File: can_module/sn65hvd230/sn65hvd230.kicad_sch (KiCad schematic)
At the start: 5 parts, among them J1 Conn_01x04, J2 Conn_01x02, U1 SN65HVD230

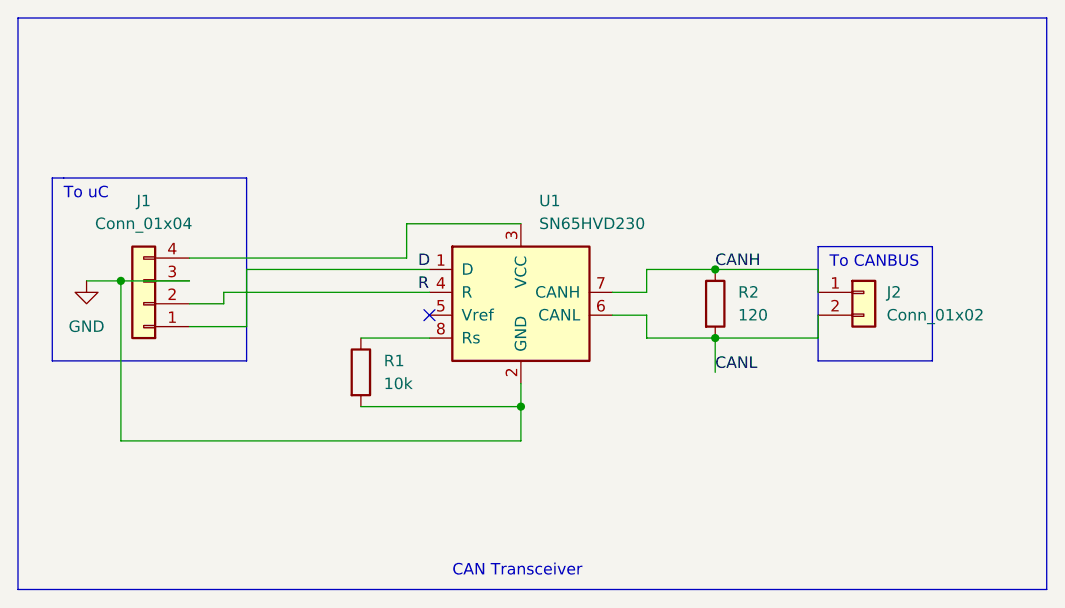
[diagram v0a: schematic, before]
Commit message: updated to use heiarchical sheets for the main schematic
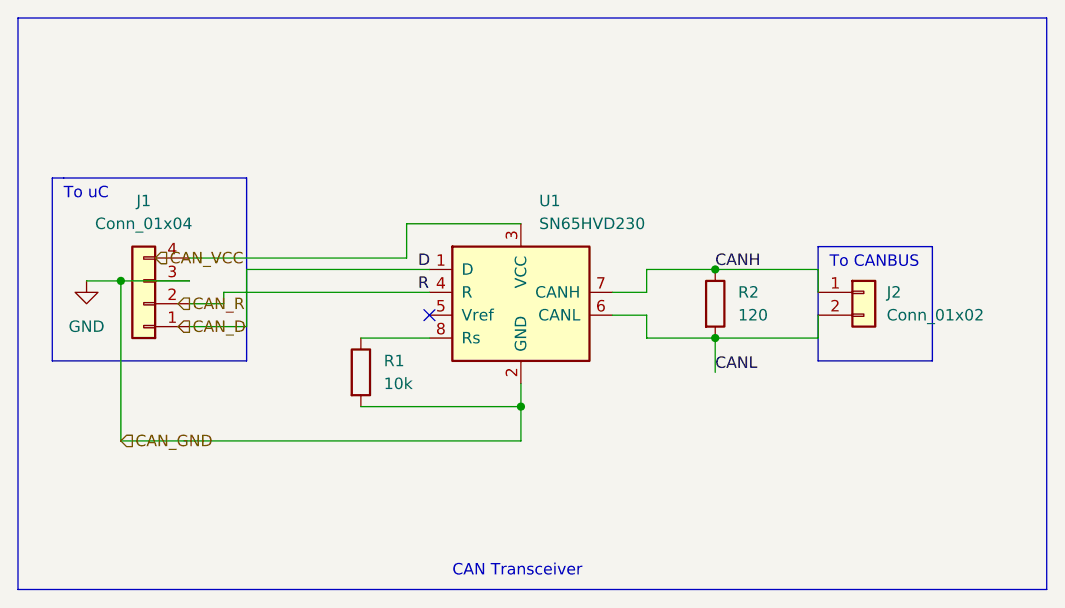
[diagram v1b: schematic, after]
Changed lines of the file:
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@@
     (effects (font (size 1.27 1.27)) (justify left bottom))
+  )
+  (hierarchical_label "CAN_D" (shape input) (at 119.38 97.79 0)
+    (effects (font (size 1.27 1.27)) (justify left))
+  )
+  (hierarchical_label "CAN_R" (shape input) (at 119.38 95.25 0)
+    (effects (font (size 1.27 1.27)) (justify left))
+  )
+  (hierarchical_label "CAN_VCC" (shape input) (at 116.84 90.17 0)
+    (effects (font (size 1.27 1.27)) (justify left))
+  )
+  (hierarchical_label "CAN_GND" (shape input) (at 113.03 110.49 0)
+    (effects (font (size 1.27 1.27)) (justify left))
   )
   (symbol (lib_id "Interface_CAN_LIN:SN65HVD230") (at 157.48 93.98 0) (unit 1)

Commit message: updated the network labels along with global nets. Also added programming/debugging port to schematic.
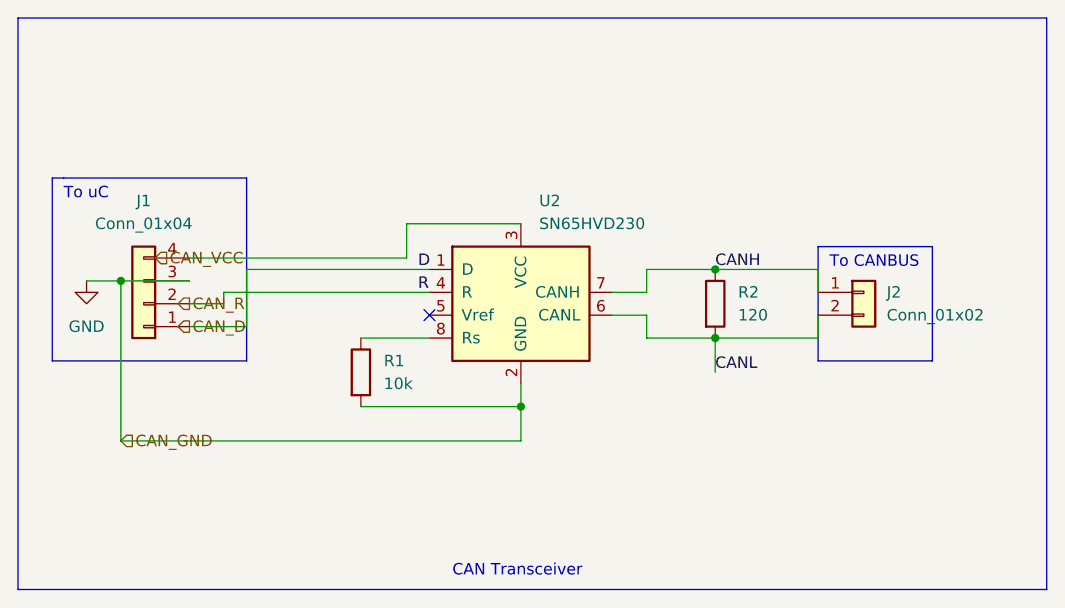
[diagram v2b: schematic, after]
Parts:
- renumbered U1 to U2
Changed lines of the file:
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@@
   (symbol (lib_id "Interface_CAN_LIN:SN65HVD230") (at 157.48 93.98 0) (unit 1)
     (in_bom yes) (on_board yes) (fields_autoplaced)
-    (property "Reference" "U1" (id 0) (at 159.4994 83.82 0)
+    (property "Reference" "U2" (id 0) (at 159.4994 83.82 0)
       (effects (font (size 1.27 1.27)) (justify left))
     )

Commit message: fixed some connection issues, and imported the bluepill module
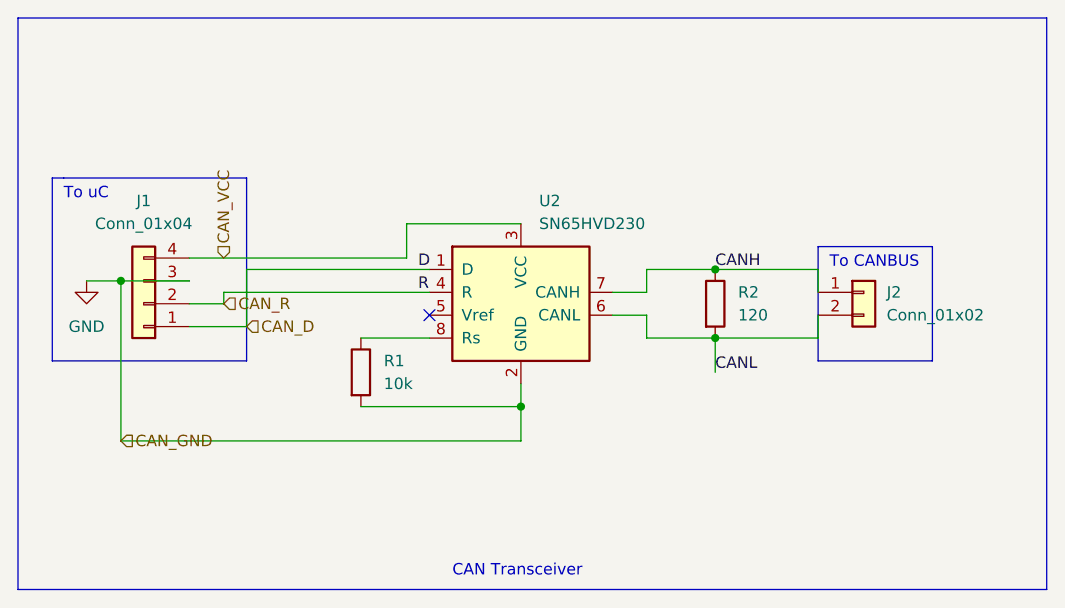
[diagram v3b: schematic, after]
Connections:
- net D is gone; now on net CAN_D: J1.1 (Pin_1), U2.1 (D)
- net R is gone; now on net CAN_R: J1.2 (Pin_2), U2.4 (R)
- net CAN_VCC: now also J1.4 (Pin_4), U2.3 (VCC)
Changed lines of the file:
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@@
     (effects (font (size 1.27 1.27)) (justify left bottom))
   )
-  (hierarchical_label "CAN_D" (shape input) (at 119.38 97.79 0)
+  (hierarchical_label "CAN_D" (shape input) (at 127 97.79 0)
     (effects (font (size 1.27 1.27)) (justify left))
   )
-  (hierarchical_label "CAN_R" (shape input) (at 119.38 95.25 0)
+  (hierarchical_label "CAN_R" (shape input) (at 124.46 95.25 0)
     (effects (font (size 1.27 1.27)) (justify left))
   )
-  (hierarchical_label "CAN_VCC" (shape input) (at 116.84 90.17 0)
+  (hierarchical_label "CAN_VCC" (shape input) (at 124.46 90.17 90)
     (effects (font (size 1.27 1.27)) (justify left))
   )

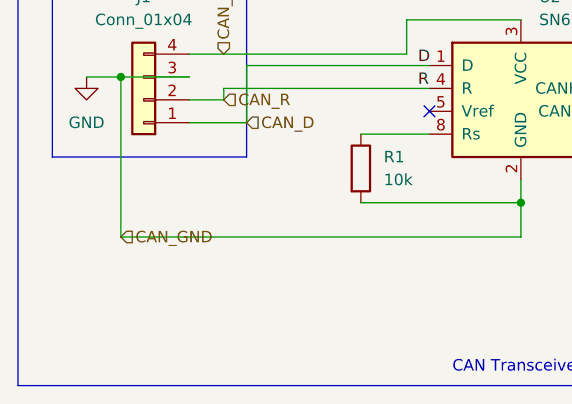
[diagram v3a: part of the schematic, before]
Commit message: fixed two more errors with electrical rules check
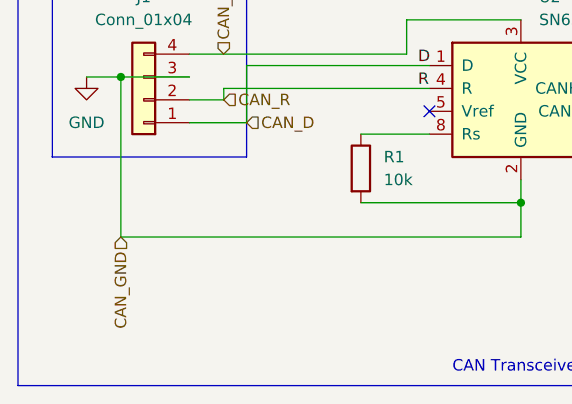
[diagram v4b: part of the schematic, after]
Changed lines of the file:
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@@
     (effects (font (size 1.27 1.27)) (justify left))
   )
-  (hierarchical_label "CAN_GND" (shape input) (at 113.03 110.49 0)
-    (effects (font (size 1.27 1.27)) (justify left))
+  (hierarchical_label "CAN_GND" (shape input) (at 113.03 110.49 270)
+    (effects (font (size 1.27 1.27)) (justify right))
   )
   (symbol (lib_id "Interface_CAN_LIN:SN65HVD230") (at 157.48 93.98 0) (unit 1)

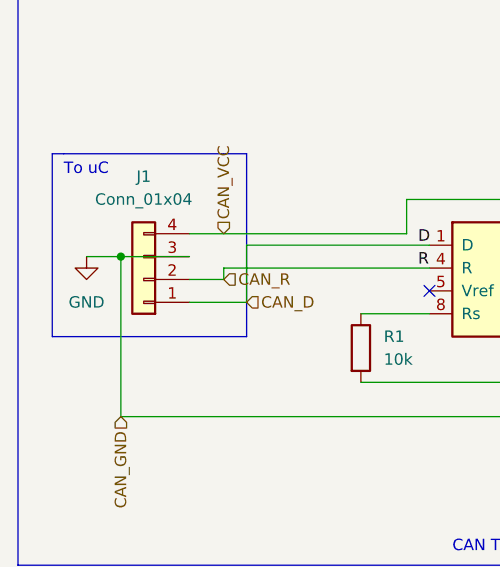
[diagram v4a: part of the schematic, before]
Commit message: added power flags to sn665hvd230
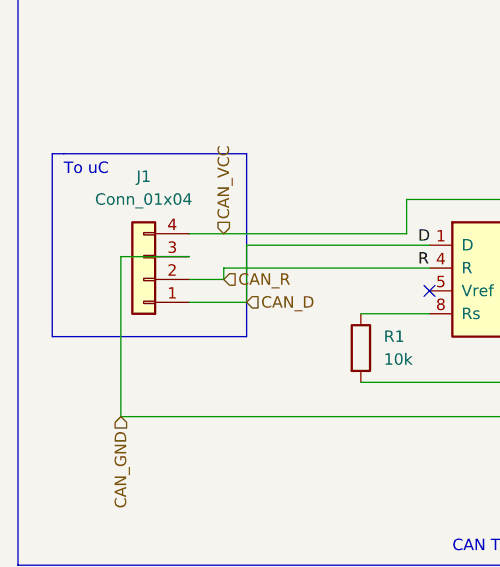
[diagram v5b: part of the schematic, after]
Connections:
- net GND renamed CAN_GND
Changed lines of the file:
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@@
   (junction (at 157.48 106.68) (diameter 0) (color 0 0 0 0)
-  )
-  (junction (at 113.03 92.71) (diameter 0) (color 0 0 0 0)
   )
   (no_connect (at 147.32 96.52))
@@
   )
   (wire (pts (xy 179.07 102.87) (xy 179.07 99.06))
-    (stroke (width 0) (type default) (color 0 0 0 0))
-  )
-  (wire (pts (xy 109.22 92.71) (xy 113.03 92.71))
     (stroke (width 0) (type default) (color 0 0 0 0))
   )
@@
     (pin "2")
   )
-  (symbol (lib_id "power:GND") (at 109.22 92.71 0) (unit 1)
-    (in_bom yes) (on_board yes) (fields_autoplaced)
-    (property "Reference" "#PWR01" (id 0) (at 109.22 99.06 0)
-      (effects (font (size 1.27 1.27)) hide)
-    )
-    (property "Value" "GND" (id 1) (at 109.22 97.79 0))
-    (property "Footprint" "" (id 2) (at 109.22 92.71 0)
-      (effects (font (size 1.27 1.27)) hide)
-    )
-    (property "Datasheet" "" (id 3) (at 109.22 92.71 0)
-      (effects (font (size 1.27 1.27)) hide)
-    )
-    (pin "1")
-  )
   (symbol (lib_id "Connector_Generic:Conn_01x04") (at 115.57 95.25 180) (unit 1)

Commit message: updated
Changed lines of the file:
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@@
   (junction (at 157.48 106.68) (diameter 0) (color 0 0 0 0)
+  )
+  (junction (at 135.89 90.17) (diameter 0) (color 0 0 0 0)
   )
   (no_connect (at 147.32 96.52))
@@
     (stroke (width 0) (type default) (color 0 0 0 0))
   )
+  (wire (pts (xy 135.89 90.17) (xy 144.78 90.17))
+    (stroke (width 0) (type default) (color 0 0 0 0))
+  )
   (wire (pts (xy 179.07 102.87) (xy 179.07 99.06))
     (stroke (width 0) (type default) (color 0 0 0 0))
@@
     (stroke (width 0) (type default) (color 0 0 0 0))
   )
+  (wire (pts (xy 135.89 88.9) (xy 135.89 90.17))
+    (stroke (width 0) (type default) (color 0 0 0 0))
+  )
   (polyline (pts (xy 215.9 127) (xy 101.6 127))
     (stroke (width 0) (type default) (color 0 0 0 0))
@@
     (stroke (width 0) (type default) (color 0 0 0 0))
   )
-  (wire (pts (xy 120.65 90.17) (xy 144.78 90.17))
+  (wire (pts (xy 120.65 90.17) (xy 135.89 90.17))
     (stroke (width 0) (type default) (color 0 0 0 0))
   )
@@
     (pin "2")
   )
+  (symbol (lib_id "power:PWR_FLAG") (at 135.89 88.9 0) (unit 1)
+    (in_bom yes) (on_board yes) (fields_autoplaced)
+    (property "Reference" "#FLG0102" (id 0) (at 135.89 86.995 0)
+      (effects (font (size 1.27 1.27)) hide)
+    )
+    (property "Value" "PWR_FLAG" (id 1) (at 135.89 83.82 0))
+    (property "Footprint" "" (id 2) (at 135.89 88.9 0)
+      (effects (font (size 1.27 1.27)) hide)
+    )
+    (property "Datasheet" "~" (id 3) (at 135.89 88.9 0)
+      (effects (font (size 1.27 1.27)) hide)
+    )
+    (pin "1")
+  )
   (sheet_instances
